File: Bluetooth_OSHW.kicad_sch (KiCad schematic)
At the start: 0 parts

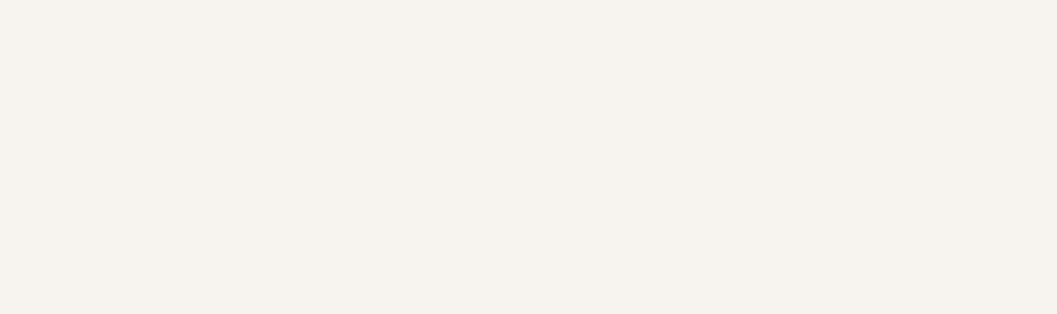
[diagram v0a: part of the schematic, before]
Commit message: removed backup zips. adding updated output files
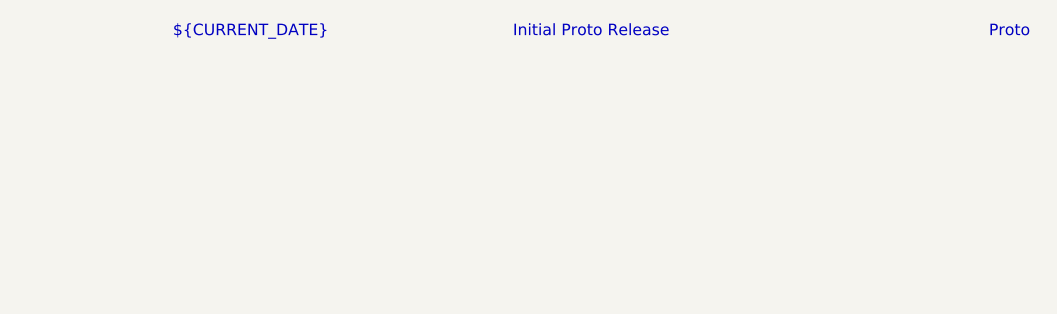
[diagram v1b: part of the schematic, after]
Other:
- note added: "${CURRENT_DATE}"
- note added: "Initial Proto Release"
- note added: "Proto"
- title: nRF Battery Dev Kit -> stm32_bluet_pill
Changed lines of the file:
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@@
 	(paper "A3")
 	(title_block
-		(title "nRF Battery Dev Kit")
-		(date "2024-02-26")
+		(title "stm32_bluet_pill")
+		(date "2024-04-03")
 		(rev "Proto")
 		(company "Clover Designs")
 		(comment 1 "Brendan Bleker")
 	)
+	(text "Proto"
+		(exclude_from_sim no)
+		(at 389.636 18.288 0)
+		(effects
+			(font
+				(size 1.27 1.27)
+			)
+		)
+	)
+	(text "${CURRENT_DATE}"
+		(exclude_from_sim no)
+		(at 305.308 18.288 0)
+		(effects
+			(font
+				(size 1.27 1.27)
+			)
+		)
+	)
+	(text "Initial Proto Release"
+		(exclude_from_sim no)
+		(at 343.154 18.288 0)
+		(effects
+			(font
+				(size 1.27 1.27)
+			)
+		)
+	)
 	(sheet
